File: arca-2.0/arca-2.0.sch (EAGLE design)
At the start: 20 parts

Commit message: drivers
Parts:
- added CON_BATTERY, CON_DRV1, CON_DRV2, CON_DRV3, CON_DRV4, CON_DRV5, CON_DRV6: LPTA-2POS, con-phoenix-5mm:LPTA-2POS
- added D10, D5, D6, D7, D8, D9: SS54, diode-ss:SS54
- added D4: (no value), diode:DIODE-DO201-15
- added DRV_STAT_1, DRV_STAT_2, DRV_STAT_3, DRV_STAT_4, DRV_STAT_5, DRV_STAT_6, FS_STAT_1, FS_STAT_2, FS_STAT_3, FS_STAT_4, FS_STAT_5, FS_STAT_6: (no value), led:LEDCHIPLED_1206
- added FS1, FS2, FS3, FS4, FS5, FS6: 178.6165, fuse-holder-littlefuse:178.6165
- added PWR_12V: RED, led:LEDCHIPLED_1206
- added R10, R13, R16, R19, R22, R7: 10k, rcl:R-US_R1206
- added R11, R12, R14, R15, R17, R18, R20, R21, R23, R24, R8, R9: 220, rcl:R-US_R1206
- added R6: 300, rcl:R-US_R1206
- added SW1: 1101M2S3CQE2, switch-slide:1101M2S3CQE2
- added T1, T2, T3, T4, T5, T6: FQP30N06L, transistor-FQP:FQP30N06L
- C5: value (none) -> 10u
- R1: value 10k -> 68k
- R2: value 1.5k -> 10k
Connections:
- new net 12V_CON: CON_BATTERY_1.SK, SW1.P
- new net 12V_IN: D4.A, SW1.O
- new net DRV_CTL_1: R7.2, T1.G
- new net DRV_CTL_2: R10.2, T2.G
- new net DRV_CTL_3: R13.2, T3.G
- new net DRV_CTL_4: R16.2, T4.G
- new net DRV_CTL_5: R19.2, T5.G
- new net DRV_CTL_6: R22.2, T6.G
- new net DRV_NEG_1: CON_DRV1_2.SK, D5.P$2, R9.1, T1.D
- new net DRV_NEG_2: CON_DRV2_2.SK, D6.P$2, R12.1, T2.D
- new net DRV_NEG_3: CON_DRV3_2.SK, D7.P$2, R15.1, T3.D
- new net DRV_NEG_4: CON_DRV4_2.SK, D8.P$2, R18.1, T4.D
- new net DRV_NEG_5: CON_DRV5_2.SK, D9.P$2, R21.1, T5.D
- new net DRV_NEG_6: CON_DRV6_2.SK, D10.P$2, R24.1, T6.D
- new net DRV_POS_1: CON_DRV1_1.SK, D5.P$1, DRV_STAT_1.A, FS1.1, FS_STAT_1.A
- new net DRV_POS_2: CON_DRV2_1.SK, D6.P$1, DRV_STAT_2.A, FS2.1, FS_STAT_2.A
- new net DRV_POS_3: CON_DRV3_1.SK, D7.P$1, DRV_STAT_3.A, FS3.1, FS_STAT_3.A
- new net DRV_POS_4: CON_DRV4_1.SK, D8.P$1, DRV_STAT_4.A, FS4.1, FS_STAT_4.A
- new net DRV_POS_5: CON_DRV5_1.SK, D9.P$1, DRV_STAT_5.A, FS5.1, FS_STAT_5.A
- new net DRV_POS_6: CON_DRV6_1.SK, D10.P$1, DRV_STAT_6.A, FS6.1, FS_STAT_6.A
- new net N$1: FS_STAT_2.C, R11.2
- new net N$10: DRV_STAT_3.C, R15.2
- new net N$11: FS_STAT_4.C, R17.2
- new net N$12: DRV_STAT_4.C, R18.2
- new net N$13: FS_STAT_5.C, R20.2
- new net N$14: DRV_STAT_5.C, R21.2
- new net N$15: FS_STAT_6.C, R23.2
- new net N$16: DRV_STAT_6.C, R24.2
- new net N$5: PWR_12V.C, R6.2
- new net N$6: DRV_STAT_2.C, R12.2
- new net N$7: FS_STAT_3.C, R14.2
- new net N$8: FS_STAT_1.C, R8.2
- new net N$9: DRV_STAT_1.C, R9.2
- net +12V: now also D4.C, FS1.2, FS2.2, FS3.2, FS4.2, FS5.2, FS6.2, PWR_12V.A
- net GND: now also CON_BATTERY_2.SK, R10.1, R11.1, R13.1, R14.1, R16.1, R17.1, R19.1, R20.1, R22.1, R23.1, R6.1, R7.1, R8.1, T1.S, T2.S, T3.S, T4.S, T5.S, T6.S
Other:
- note added: "Driver 6 is ignition"
- note added: "Voltage Regulation"

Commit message: started on LC work
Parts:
- added C10, C7, C8, C9: 1u, rcl:C-USC1206
- added C11: 0.1u, rcl:C-USC1206
- added C12, C13, C14, C15: 1n, rcl:C-USC1206
- added CON_LC1, CON_LC2, CON_LC3, CON_LC4: LPTA-4POS, con-phoenix-5mm:LPTA-4POS
- added IC1, IC2, IC3, IC4: MCP6N11R, inamp-microchip:MCP6N11R
- added IC5: LM324D, linear:LM324D
- added R25, R29: 39k, rcl:R-US_R1206
- added R26, R30: 10k, rcl:R-US_R1206
- added R27, R28, R31, R32: 62k, rcl:R-US_R1206
- added RF1, RF2, RF3, RF4, RG1, RG2, RG3, RG4: (no value), rcl:R-US_R1206
- added RZ1, RZ2, RZ3, RZ4: (no value), pot:TRIM_US-S64W
- C6: value (none) -> 10u
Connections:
- new net LC1+: CON_LC1_2.SK, IC1.+
- new net LC1-: CON_LC1_3.SK, IC1.-
- new net LC1_CAL: C12.2, IC5A.OUT, R25.2
- new net LC1_PREC: IC1.OUT, R28.1
- new net LC2+: CON_LC2_2.SK, IC2.+
- new net LC2-: CON_LC2_3.SK, IC2.-
- new net LC2_CAL: C14.2, R29.2
- new net LC2_PREC: IC2.OUT, R32.1
- new net LC3+: CON_LC3_2.SK, IC3.+
- new net LC3-: CON_LC3_3.SK, IC3.-
- new net LC3_PREC: IC3.OUT
- new net LC4+: CON_LC4_2.SK, IC4.+
- new net LC4-: CON_LC4_3.SK, IC4.-
- new net LC4_PREC: IC4.OUT
- new net LC_EN: IC1.EN, IC2.EN, IC3.EN, IC4.EN
- new net N$17: IC1.REF, RF1.1, RG1.2
- new net N$18: IC1.FG, RF1.2
- new net N$19: RG1.1, RZ1.S
- new net N$20: IC2.REF, RF2.1, RG2.2
- new net N$21: IC2.FG, RF2.2
- new net N$22: RG2.1, RZ2.S
- new net N$23: IC3.REF, RF3.1, RG3.2
- new net N$24: IC3.FG, RF3.2
- new net N$25: RG3.1, RZ3.S
- new net N$26: IC4.REF, RF4.1, RG4.2
- new net N$27: IC4.FG, RF4.2
- new net N$28: RG4.1, RZ4.S
- new net N$29: IC5A.-IN, R25.1, R26.2
- new net N$30: R29.1, R30.2
- new net N$31: C13.1, IC5A.+IN, R27.2
- new net N$32: C12.1, R27.1, R28.2
- new net N$33: C15.1, R31.2
- new net N$34: C14.1, R31.1, R32.2
- net +10V: now also CON_LC1_1.SK, CON_LC2_1.SK, CON_LC3_1.SK, CON_LC4_1.SK
- net +3V3: now also C10.1, C7.1, C8.1, C9.1, IC1.+V, IC2.+V, IC3.+V, IC4.+V, RZ1.E, RZ2.E, RZ3.E, RZ4.E
- net +5V: now also C11.1, IC5P.V+
- net GND: now also C10.2, C11.2, C13.2, C15.2, C7.2, C8.2, C9.2, CON_LC1_4.SK, CON_LC2_4.SK, CON_LC3_4.SK, CON_LC4_4.SK, IC1.-V, IC2.-V, IC3.-V, IC4.-V, IC5P.V-, R26.1, R30.1, RZ1.A, RZ2.A, RZ3.A, RZ4.A
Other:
- note added: "Second-order Sallen-Key LPF. f_c = 1/(2 pi sqrt(R27 * R28 * C12 * C13)). G = 1 + (R25/R26)"
- note added: "f_c = 2.57 kHz G = 4.9"

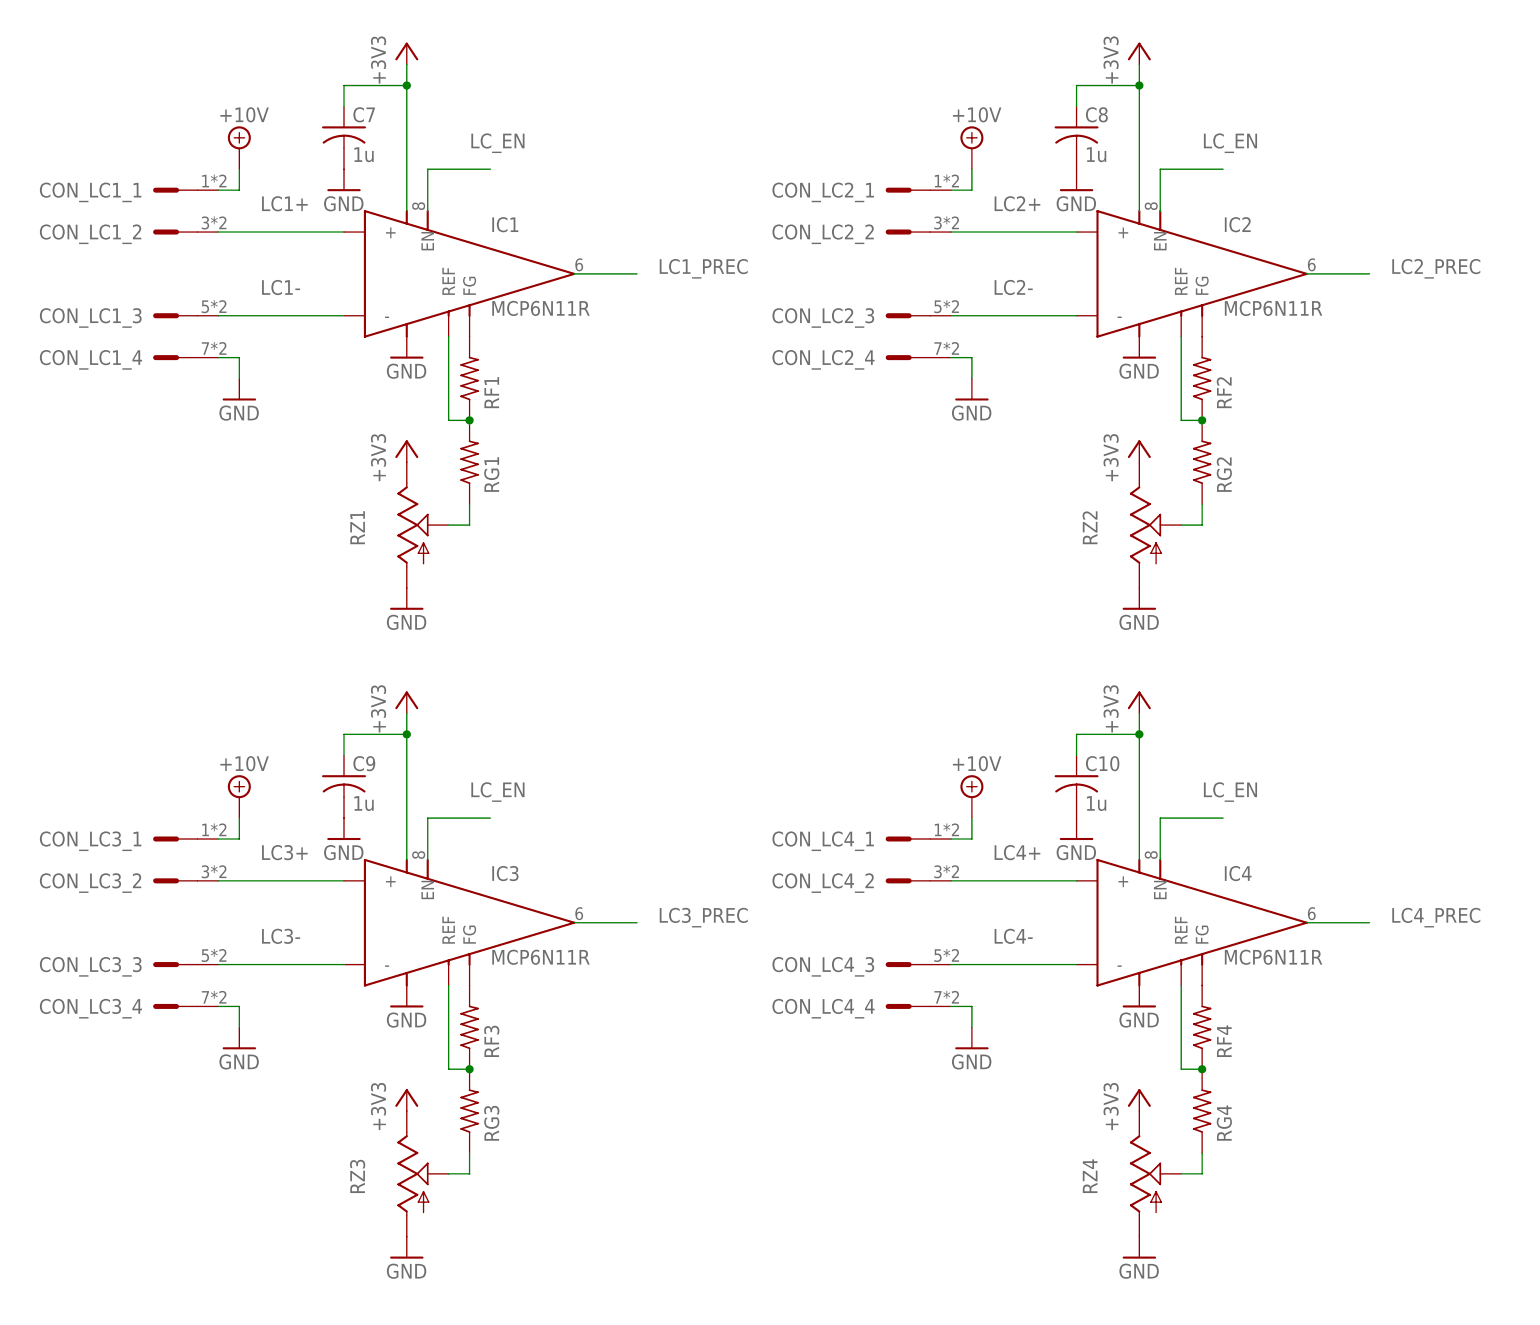
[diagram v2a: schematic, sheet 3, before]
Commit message: fixed incorrect feedback on LC inamp
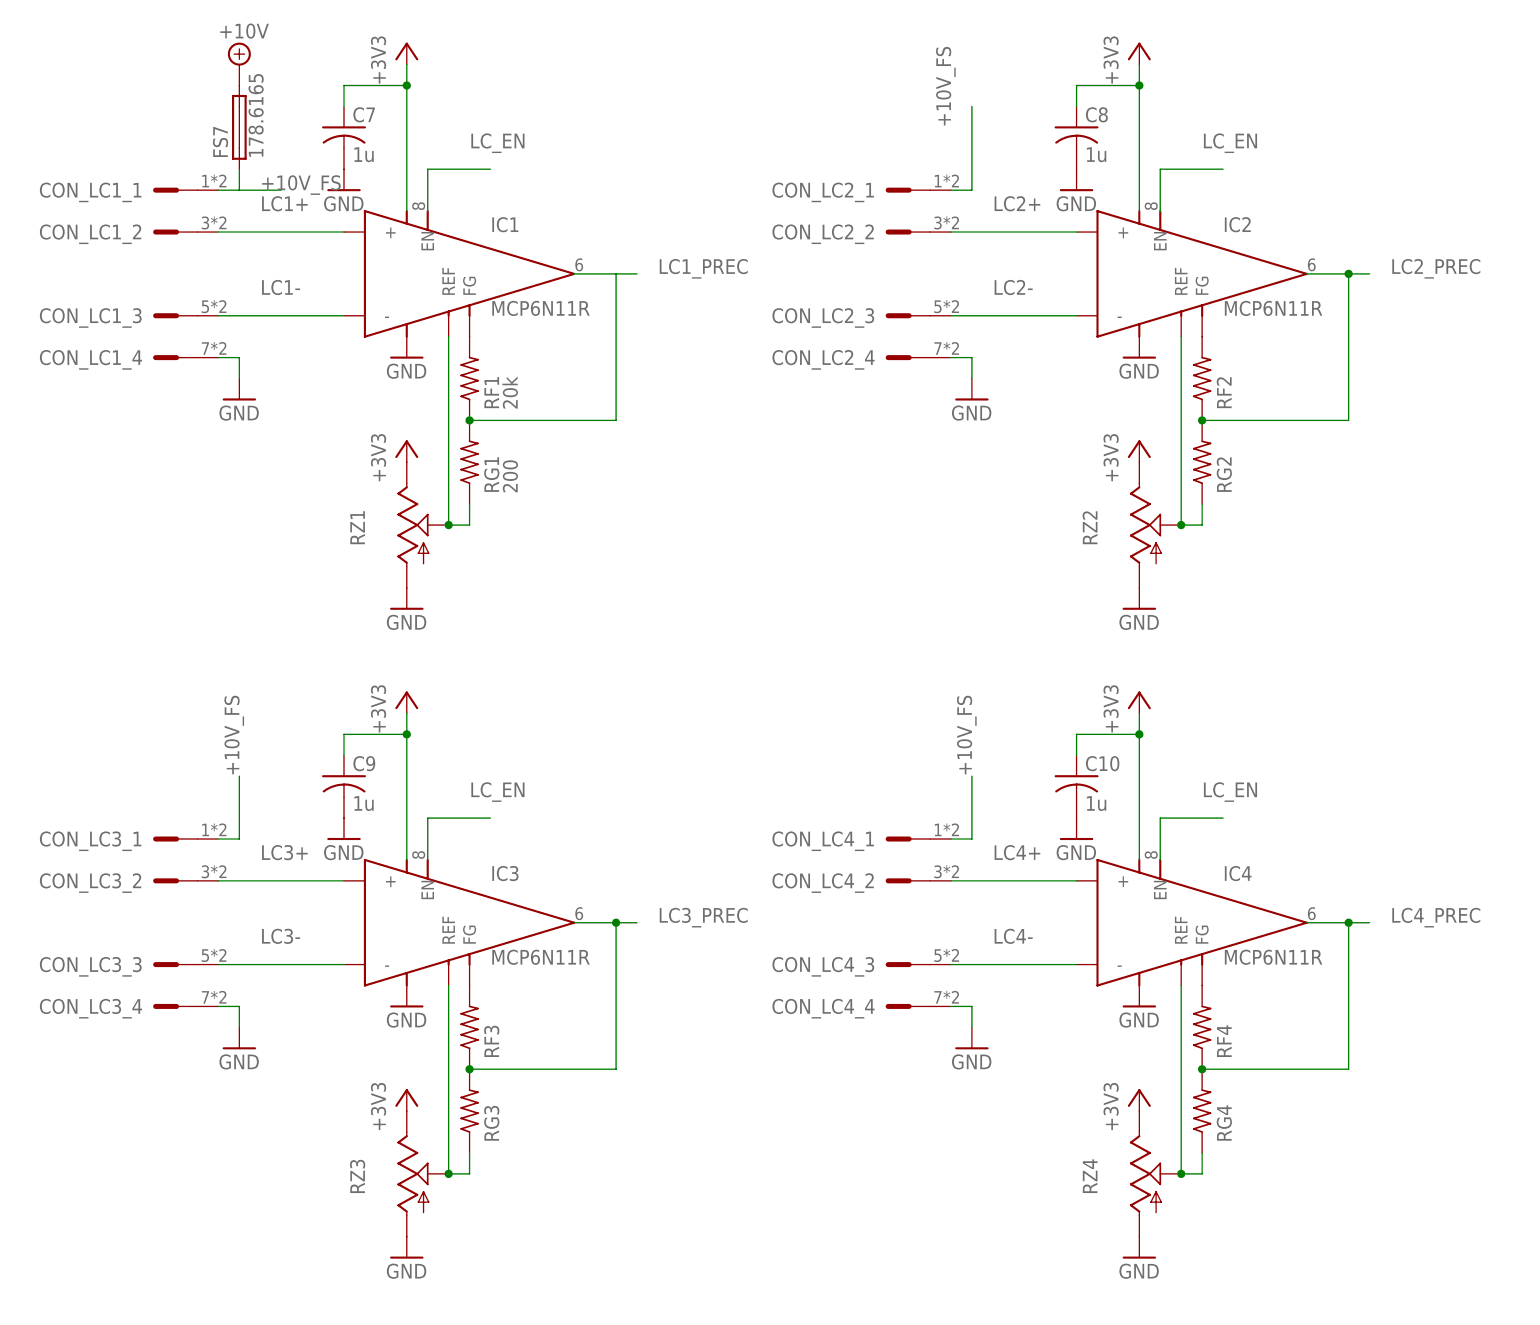
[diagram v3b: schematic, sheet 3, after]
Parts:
- added FS7: 178.6165, fuse-holder-littlefuse:178.6165
- RF1: value (none) -> 20k
- RG1: value (none) -> 200
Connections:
- removed net N$19: RG1.1, RZ1.S
- removed net N$20: IC2.REF, RF2.1, RG2.2
- removed net N$23: IC3.REF, RF3.1, RG3.2
- removed net N$26: IC4.REF, RF4.1, RG4.2
- new net +10V_FS: CON_LC1_1.SK, CON_LC2_1.SK, CON_LC3_1.SK, CON_LC4_1.SK, FS7.1
- net +10V: now also FS7.2; no longer CON_LC1_1.SK, CON_LC2_1.SK, CON_LC3_1.SK, CON_LC4_1.SK
- net LC1_PREC: now also RF1.1, RG1.2
- net LC2_PREC: now also RF2.1, RG2.2
- net LC3_PREC: now also RF3.1, RG3.2
- net LC4_PREC: now also RF4.1, RG4.2
- net N$17: now also RG1.1, RZ1.S; no longer RF1.1, RG1.2
- net N$22: now also IC2.REF
- net N$25: now also IC3.REF
- net N$28: now also IC4.REF

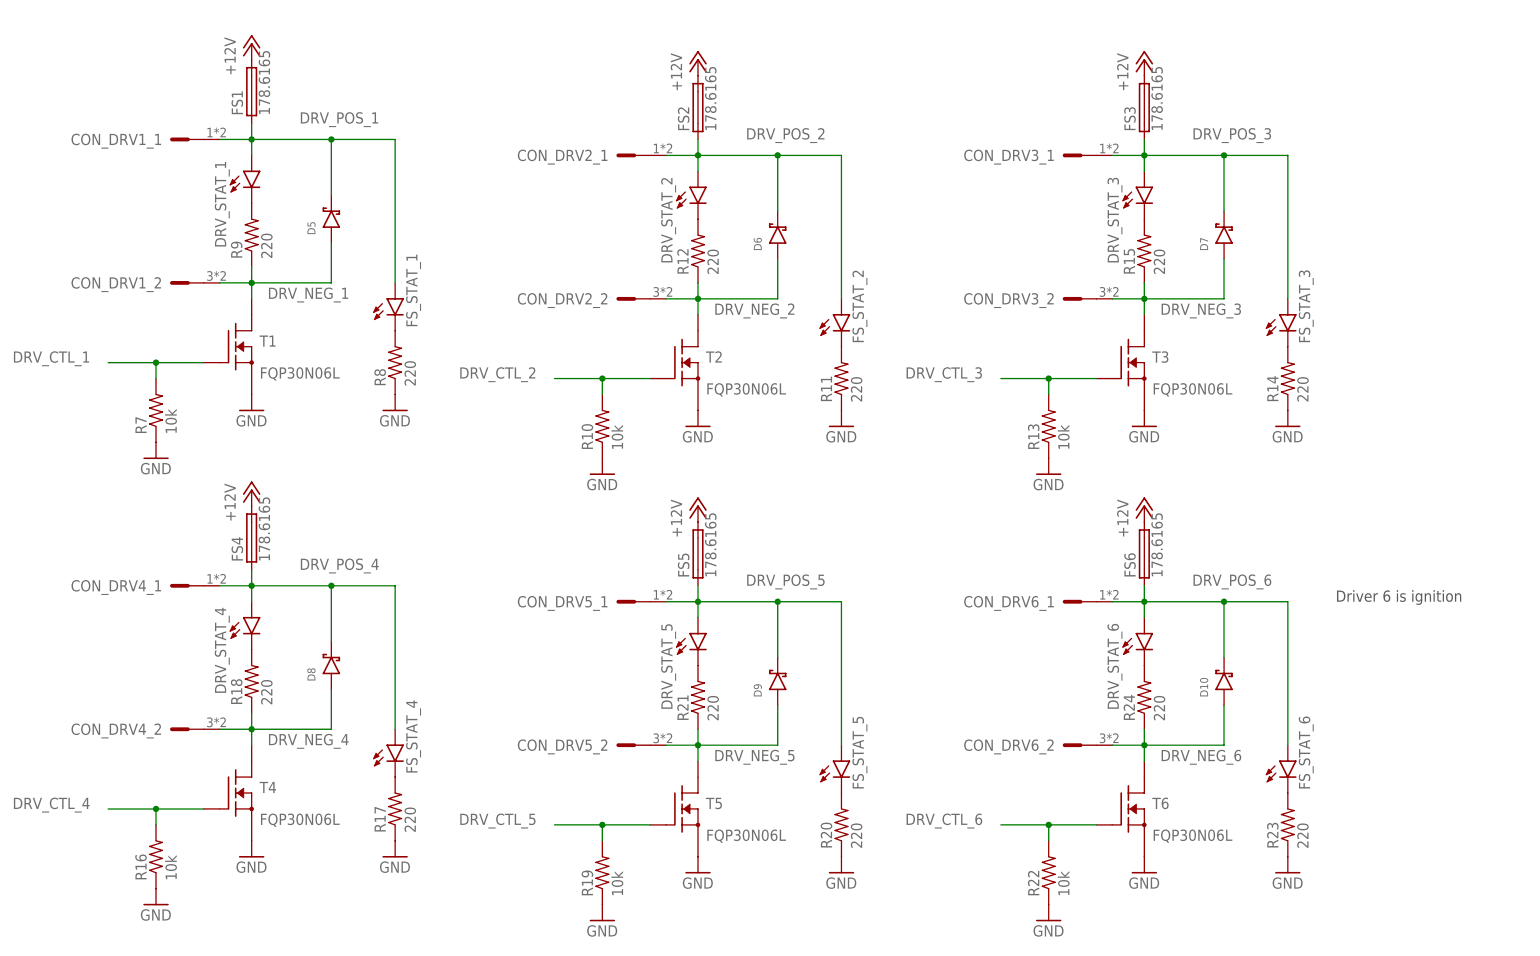
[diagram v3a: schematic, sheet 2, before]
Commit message: rip 3.3v
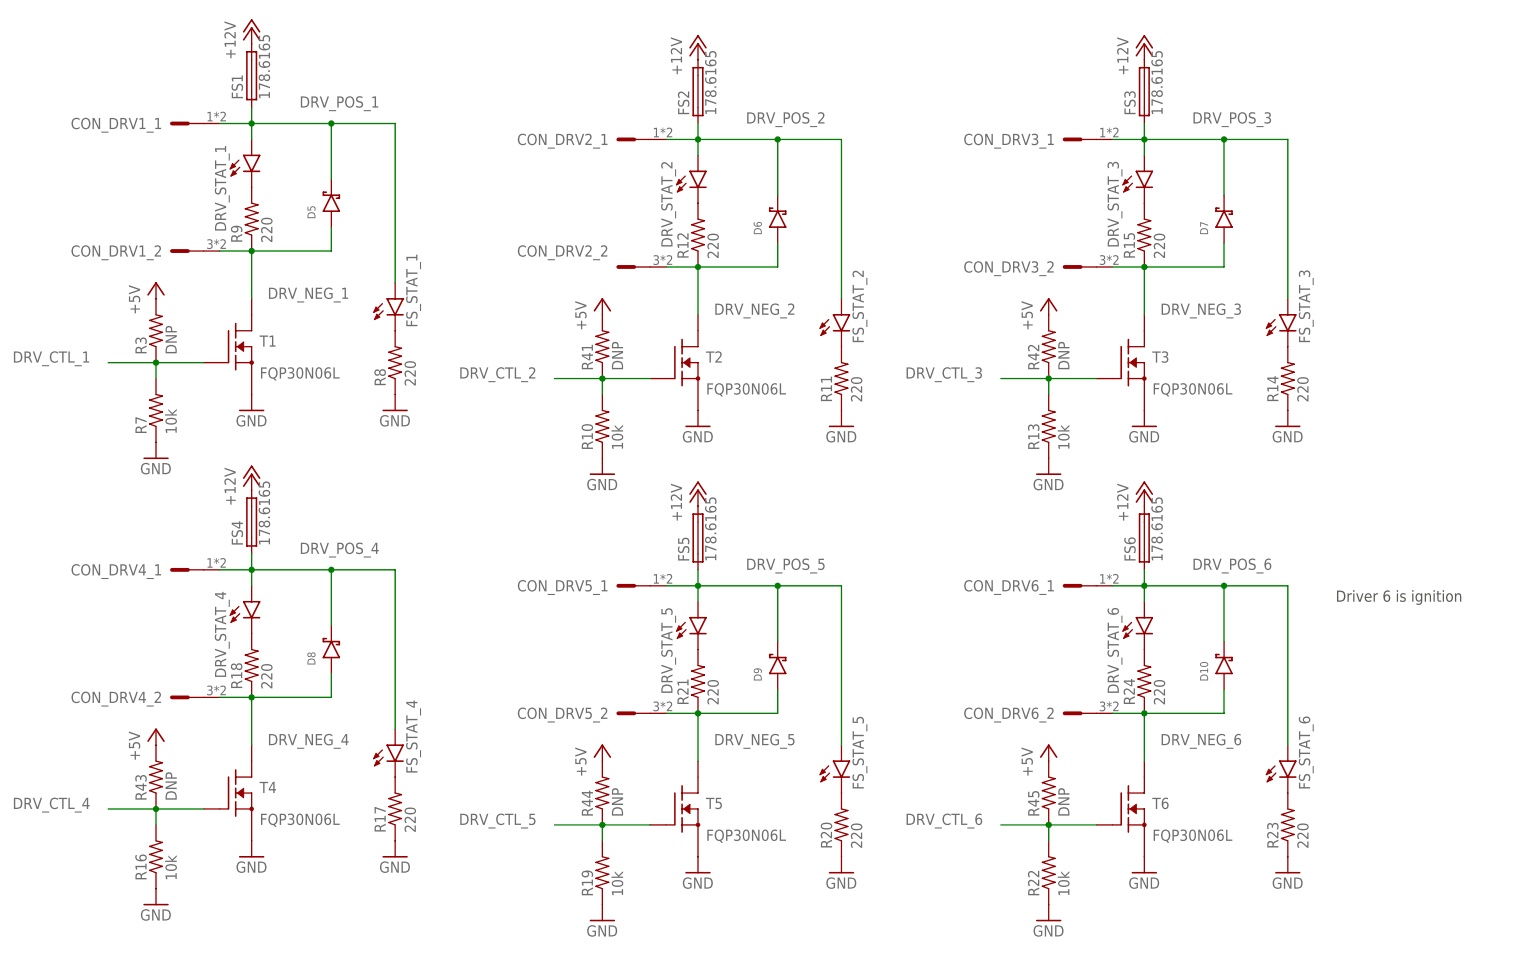
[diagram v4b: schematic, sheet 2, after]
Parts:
- removed C1, C2: 10u, rcl:C-USC1206
- removed D1: SS54, diode-ss:SS54
- removed PWR_3V3: RED, led:LEDCHIPLED_1206
- removed VR1: +3.3, LM1084:LM1084
- added C16, C17, C18, C19: 1n, rcl:C-USC1206
- added R33, R37: 39k, rcl:R-US_R1206
- added R34, R38: 10k, rcl:R-US_R1206
- added R35, R36, R39, R40: 62k, rcl:R-US_R1206
- added R41, R42, R43, R44, R45: DNP, rcl:R-US_R1206
- R27, R28: value 62k -> 56k
- R3: value 10 -> DNP
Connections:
- removed net LC_EN: IC1.EN, IC2.EN, IC3.EN, IC4.EN
- removed net N$2: PWR_3V3.C, R3.2
- new net LC3_CAL: C16.2, IC5C.OUT, R33.2
- new net LC4_CAL: C18.2, IC5D.OUT, R37.2
- new net N$19: IC5C.-IN, R33.1, R34.2
- new net N$20: C17.1, IC5C.+IN, R35.2
- new net N$23: C16.1, R35.1, R36.2
- new net N$26: IC5D.-IN, R37.1, R38.2
- new net N$35: C19.1, IC5D.+IN, R39.2
- new net N$36: C18.1, R39.1, R40.2
- net +12V: no longer C2.1, D1.P$1, VR1.VIN
- net +3V3: no longer C1.1, C10.1, C7.1, C8.1, C9.1, D1.P$2, IC1.+V, IC2.+V, IC3.+V, IC4.+V, PWR_3V3.A, VR1.VO
- net +5V: now also C10.1, C7.1, C8.1, C9.1, IC1.+V, IC1.EN, IC2.+V, IC2.EN, IC3.+V, IC3.EN, IC4.+V, IC4.EN, R3.2, R41.2, R42.2, R43.2, R44.2, R45.2
- net DRV_CTL_1: now also R3.1
- net DRV_CTL_2: now also R41.1
- net DRV_CTL_3: now also R42.1
- net DRV_CTL_4: now also R43.1
- net DRV_CTL_5: now also R44.1
- net DRV_CTL_6: now also R45.1
- net GND: now also C17.2, C19.2, R34.1, R38.1; no longer C1.2, C2.2, R3.1, VR1.GND
- net LC2_CAL: now also IC5B.OUT
- net LC3_PREC: now also R36.1
- net LC4_PREC: now also R40.1
- net N$30: now also IC5B.-IN
- net N$33: now also IC5B.+IN
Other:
- note added: "1206 LEDs typically take 2.5V forward at 30mA"
- note removed: "1206 LEDs typically take 3V forward at 30mA"
- moved on the sheet: C10, C8, CON_DRV1_1, CON_DRV1_2, CON_DRV2_1, CON_DRV2_2, CON_DRV3_1, CON_DRV3_2, CON_DRV4_1, CON_DRV4_2, CON_DRV5_1, CON_DRV5_2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
